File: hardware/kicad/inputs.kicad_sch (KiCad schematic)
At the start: 24 parts, among them U211 EL817, U221 EL817, U231 EL817, U241 EL817, U251 EL817

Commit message: Translate code, hardware and docs to English; bilingual dashboard
- tdm-logic i18n module: every dashboard text in English and Italian,
  chosen by `[display] language` in the profile (English by default, the
  TDM 850 profile keeps Italian); number formatting per language
- Slint fixed labels moved to a `Labels` global filled from the same table;
  `tdm-dash --language en|it`; reference screens regenerated in English with
  Italian check screens
- tdmctl, tdm-dash CLI, simulator scenarios, calibration errors and tools
  print English
- KiCad sheets, WireViz harnesses, perfboard plan and CAD comments in
  English, exports regenerated with the new names
- manual, research, ADRs and READMEs translated; files renamed (docs/manual,
  docs/research, English chapter and ADR names); status markers are now
  [VERIFIED] / [TO VERIFY] / [HYPOTHESIS]

Co-Authored-By: Claude Opus 5.5 <noreply@anthropic.com>
Claude-Session: https://claude.ai/code/session_01G9D4Wshjz9MkaThp4wsrGP
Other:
- note added: "High beam"
- note added: "High beam, turn signals and illumination are active at +12 V: 4.7 kΩ → EL817 LED → ground. Neutral is active to ground (the gearbox switch grounds the wire): +12V_P → 3.3 kΩ → LED → neutral wire. Outputs active low with the Pico's internal pull-up. Wire colours and neutral logic [TO VERIFY] with the bike measurements."
- note added: "Illumination"
- note added: "Left turn signal"
- note added: "Neutral (active to ground)"
- note added: "Outputs to the Pico NEUTRAL → GP6 HIGH_BEAM → GP7 TURN_L → GP8 TURN_R → GP9 ILLUM → GP10"
- note added: "Right turn signal"
- note added: "Warning light inputs"
- note removed: "Abbaglianti"
- note removed: "Abbaglianti, frecce e illuminazione sono attivi a +12 V: 4,7 kΩ → LED dell'EL817 → massa. La folle è attiva verso massa (il contatto del cambio chiude il filo a massa): +12V_P → 3,3 kΩ → LED → filo della folle. Uscite attive basse con pull-up interno del Pico. Colori dei fili e logica della folle [DA VERIFICARE] con i rilievi sulla moto."
- note removed: "Folle (attiva verso massa)"
- note removed: "Freccia destra"
- note removed: "Freccia sinistra"
- note removed: "Illuminazione"
- note removed: "Ingressi delle spie"
- note removed: "Uscite verso il Pico NEUTRAL → GP6 HIGH_BEAM → GP7 TURN_L → GP8 TURN_R → GP9 ILLUM → GP10"
- title: Ingressi delle spie (optoaccoppiatori) -> Warning light inputs (optocouplers)
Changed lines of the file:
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@@
 	(paper "A3")
 	(title_block
-		(title "Ingressi delle spie (optoaccoppiatori)")
+		(title "Warning light inputs (optocouplers)")
 		(date "2026-10-21")
 		(rev "0.1")
 		(company "tdm-dash · CERN-OHL-P-2.0")
-		(comment 1 "Foglio 2 di 8")
-		(comment 2 "Generato da hardware/kicad/generate.py: non modificare a mano")
+		(comment 1 "Sheet 2 of 8")
+		(comment 2 "Generated by hardware/kicad/generate.py: do not edit by hand")
 	)
 	(symbol
@@
 		)
 	)
-	(text "Ingressi delle spie"
+	(text "Warning light inputs"
 		(exclude_from_sim no)
 		(at 10.16 12.7 0)
@@
 		)
 	)
-	(text "Abbaglianti, frecce e illuminazione sono attivi a +12 V: 4,7 kΩ → LED dell'EL817 → massa.\nLa folle è attiva verso massa (il contatto del cambio chiude il filo a massa):\n+12V_P → 3,3 kΩ → LED → filo della folle. Uscite attive basse con pull-up interno del Pico.\nColori dei fili e logica della folle [DA VERIFICARE] con i rilievi sulla moto."
+	(text "High beam, turn signals and illumination are active at +12 V: 4.7 kΩ → EL817 LED → ground.\nNeutral is active to ground (the gearbox switch grounds the wire):\n+12V_P → 3.3 kΩ → LED → neutral wire. Outputs active low with the Pico's internal pull-up.\nWire colours and neutral logic [TO VERIFY] with the bike measurements."
 		(exclude_from_sim no)
 		(at 10.16 17.78 0)
@@
 		)
 	)
-	(text "Abbaglianti"
+	(text "High beam"
 		(exclude_from_sim no)
 		(at 12.7 40.64 0)
@@
 		)
 	)
-	(text "Freccia sinistra"
+	(text "Left turn signal"
 		(exclude_from_sim no)
 		(at 12.7 83.82 0)
@@
 		)
 	)
-	(text "Freccia destra"
+	(text "Right turn signal"
 		(exclude_from_sim no)
 		(at 12.7 127 0)
@@
 		)
 	)
-	(text "Illuminazione"
+	(text "Illumination"
 		(exclude_from_sim no)
 		(at 12.7 170.18 0)
@@
 		)
 	)
-	(text "Folle (attiva verso massa)"
+	(text "Neutral (active to ground)"
 		(exclude_from_sim no)
 		(at 12.7 213.36 0)
@@
 		)
 	)
-	(text "Uscite verso il Pico\nNEUTRAL → GP6\nHIGH_BEAM → GP7\nTURN_L → GP8\nTURN_R → GP9\nILLUM → GP10"
+	(text "Outputs to the Pico\nNEUTRAL → GP6\nHIGH_BEAM → GP7\nTURN_L → GP8\nTURN_R → GP9\nILLUM → GP10"
 		(exclude_from_sim no)
 		(at 190.5 50.8 0)

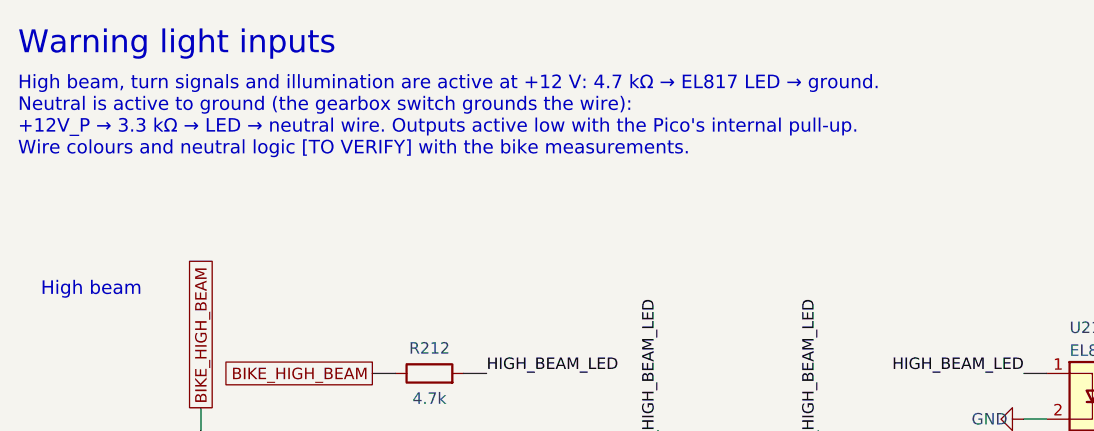
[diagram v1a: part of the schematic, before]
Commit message: English README, ADR 0012, CLAUDE.md rules, banner; consistent spelling
- README and docs/assets in English, banner tagline "Open-source digital
  instrument cluster" and regenerated banner
- ADR 0012: English repository, bilingual dashboard
- CLAUDE.md: English everywhere, dashboard texts in both languages through
  tdm-logic i18n, new status markers
- American spelling across docs, harness labels and schematic notes;
  ADR 0007 renamed to 0007-licenses; exports and screens regenerated

Co-Authored-By: Claude Opus 5.5 <noreply@anthropic.com>
Claude-Session: https://claude.ai/code/session_01G9D4Wshjz9MkaThp4wsrGP
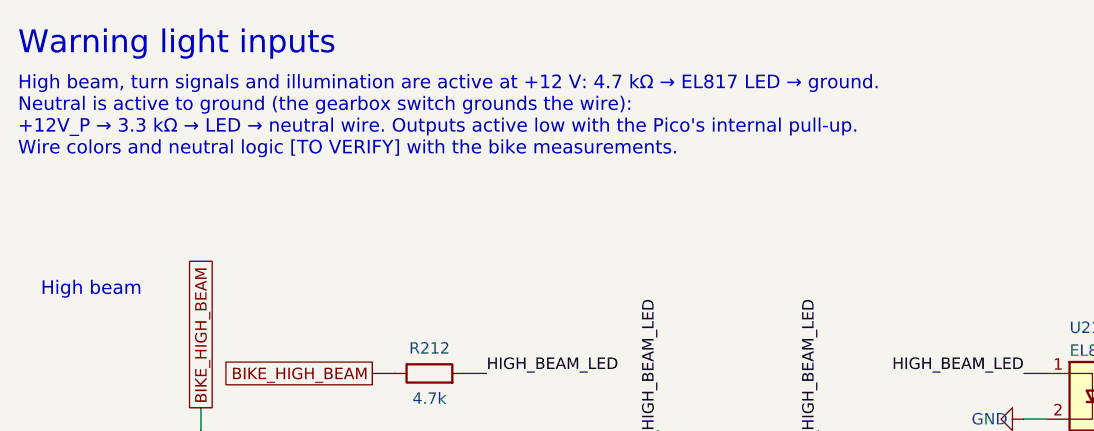
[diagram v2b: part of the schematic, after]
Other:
- note added: "High beam, turn signals and illumination are active at +12 V: 4.7 kΩ → EL817 LED → ground. Neutral is active to ground (the gearbox switch grounds the wire): +12V_P → 3.3 kΩ → LED → neutral wire. Outputs active low with the Pico's internal pull-up. Wire colors and neutral logic [TO VERIFY] with the bike measurements."
- note removed: "High beam, turn signals and illumination are active at +12 V: 4.7 kΩ → EL817 LED → ground. Neutral is active to ground (the gearbox switch grounds the wire): +12V_P → 3.3 kΩ → LED → neutral wire. Outputs active low with the Pico's internal pull-up. Wire colours and neutral logic [TO VERIFY] with the bike measurements."
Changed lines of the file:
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@@
 		)
 	)
-	(text "High beam, turn signals and illumination are active at +12 V: 4.7 kΩ → EL817 LED → ground.\nNeutral is active to ground (the gearbox switch grounds the wire):\n+12V_P → 3.3 kΩ → LED → neutral wire. Outputs active low with the Pico's internal pull-up.\nWire colours and neutral logic [TO VERIFY] with the bike measurements."
+	(text "High beam, turn signals and illumination are active at +12 V: 4.7 kΩ → EL817 LED → ground.\nNeutral is active to ground (the gearbox switch grounds the wire):\n+12V_P → 3.3 kΩ → LED → neutral wire. Outputs active low with the Pico's internal pull-up.\nWire colors and neutral logic [TO VERIFY] with the bike measurements."
 		(exclude_from_sim no)
 		(at 10.16 17.78 0)

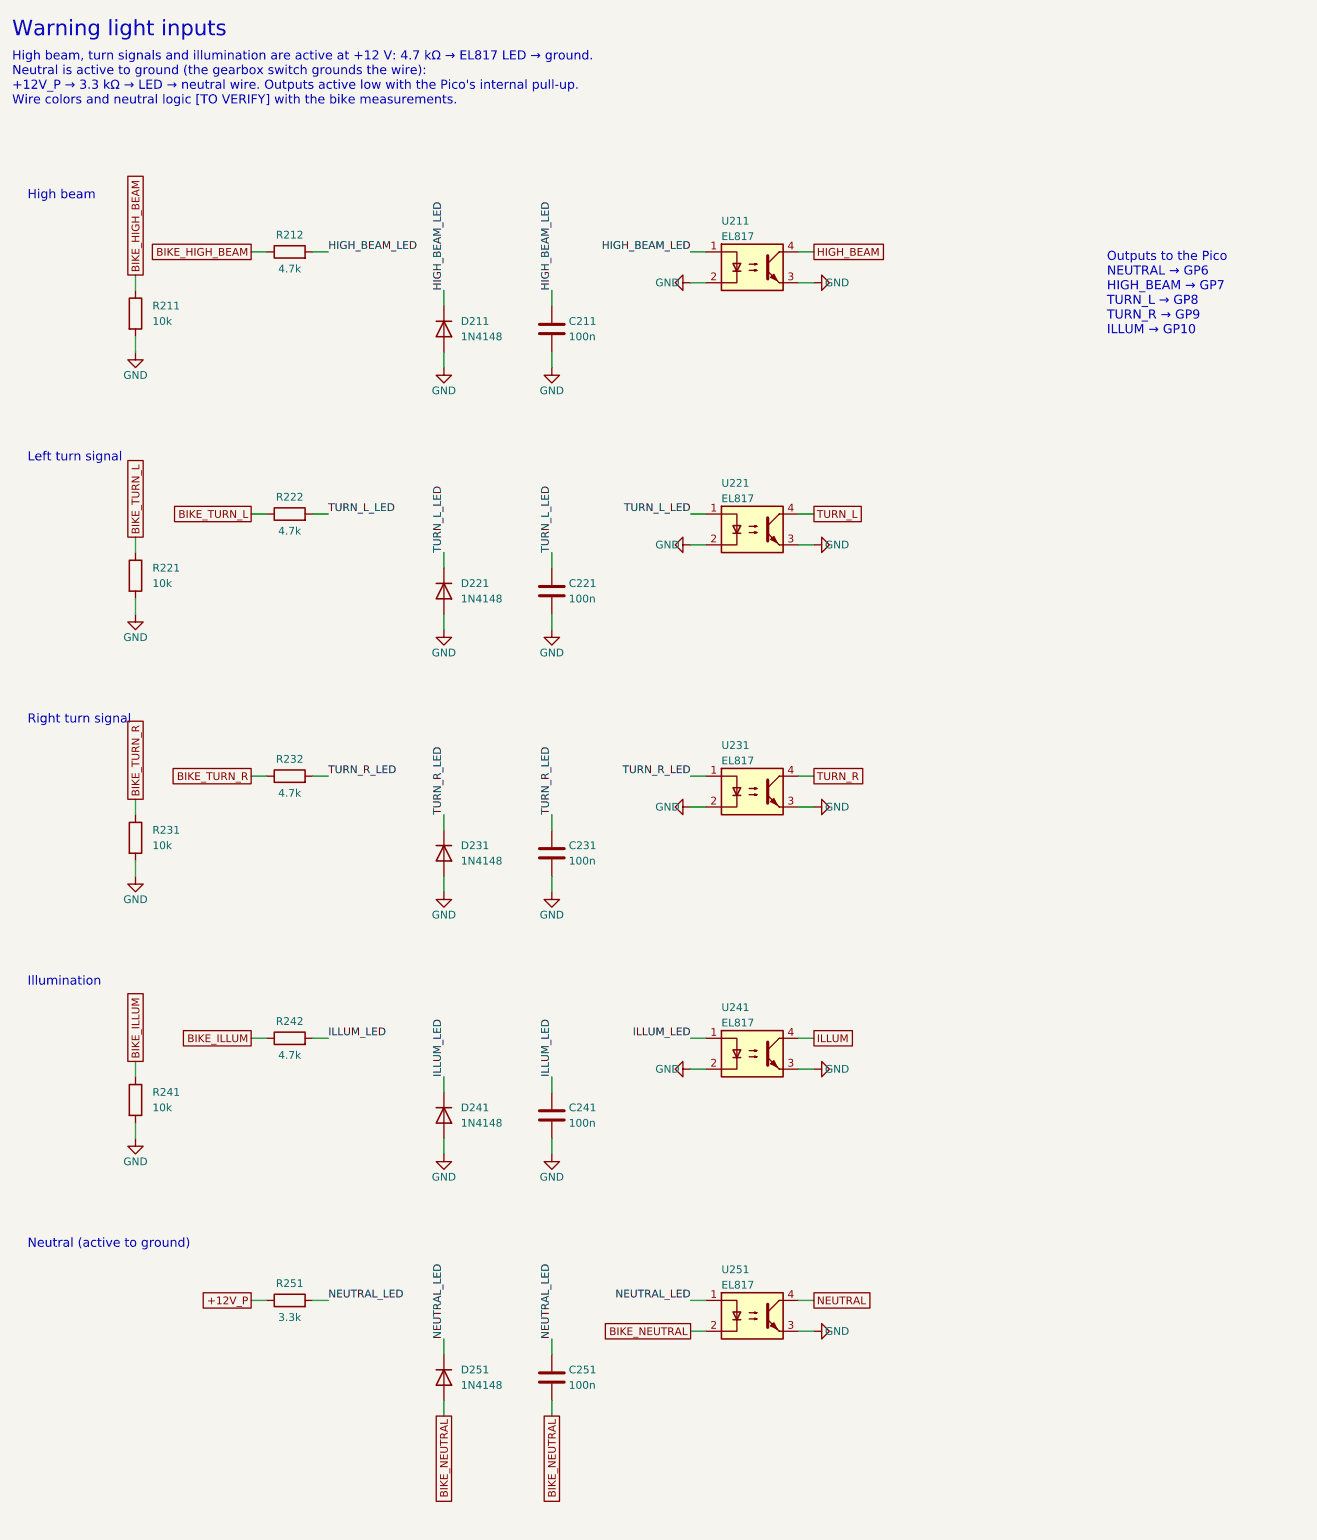
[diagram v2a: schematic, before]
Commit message: Schematic: drawn wires, block diagram, new title block
The sheets were a netlist in disguise: every pin ended in a short stub and
a label, so the circuits had to be pieced together by name, labels
overlapped, two sheets fell off the index page and the title block was
KiCad's default. The generator now draws the schematic:

- hardware/kicad/schgen: placement on the 50 mil grid, orthogonal wires,
  junctions, hierarchical ports, module and connector symbols with named
  pins; the drawing is normalised the way KiCad 9 reads it and checked
  against the declared netlist (no wire may connect anything else)
- hardware/kicad/sheets: one module per sheet, laid out left to right
  from the bike to the Pico; the root sheet is a block diagram whose
  wires are the signals between sheets
- tdm-dash.kicad_wks: frame and title block of the project
- symbols copied from KiCad 9.0.9 (vendor_symbols.py): the generator no
  longer needs KiCad installed
- export.sh: ERC, tools/check_netlist.py (KiCad's netlist is the declared
  one), check_pinmap.py, PDF and SVG on white, tools/check_svg_layout.py
  (no text over another text, a wire, the frame or the title block)

The circuit is unchanged: KiCad's netlist of the old and new schematic
has the same 56 nets (FRAM pins now follow the breakout header, R603/R604
pins swapped).

Co-Authored-By: Claude Opus 5.5 <noreply@anthropic.com>
Claude-Session: https://claude.ai/code/session_01G9D4Wshjz9MkaThp4wsrGP
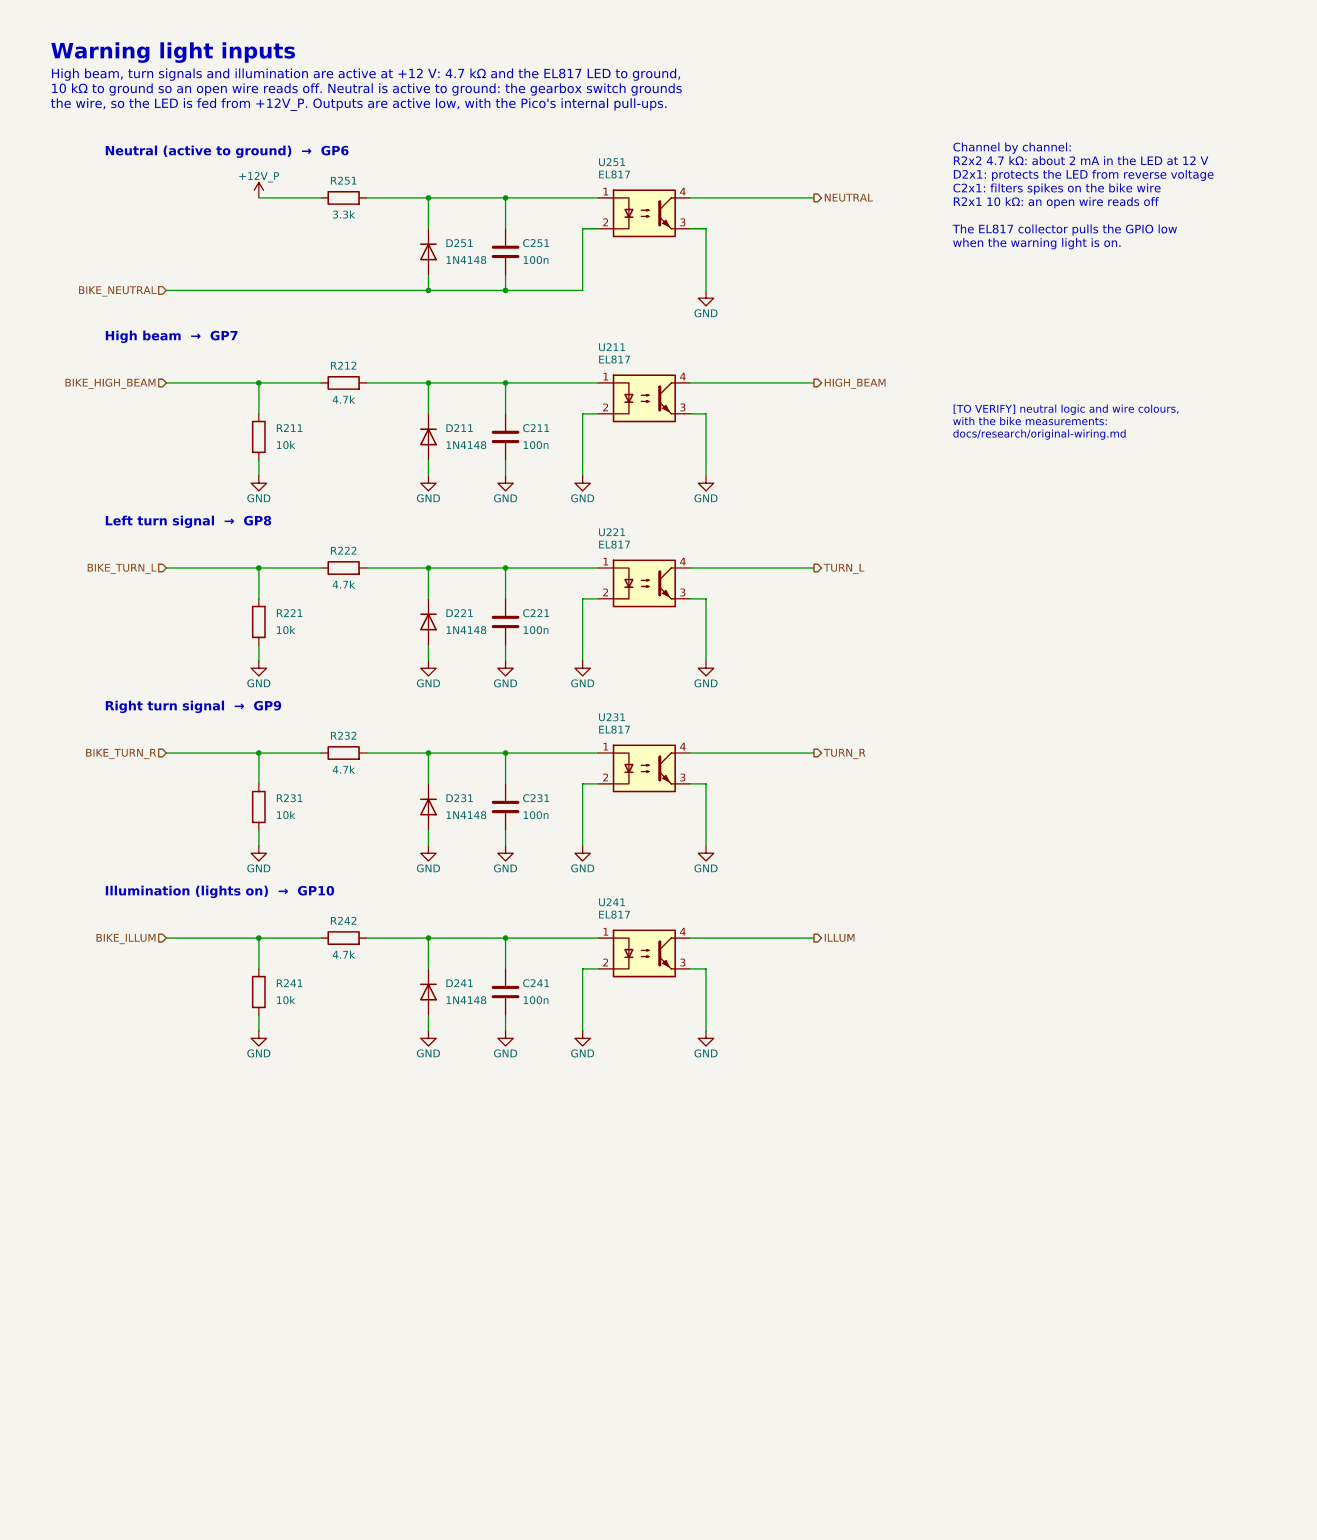
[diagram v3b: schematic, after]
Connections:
- net HIGH_BEAM_LED: no longer names the net of C211.1, D211.1 (K), R212.2, U211.1
- net ILLUM_LED: no longer names the net of C241.1, D241.1 (K), R242.2, U241.1
- net NEUTRAL_LED: no longer names the net of C251.1, D251.1 (K), R251.2, U251.1
- net TURN_L_LED: no longer names the net of C221.1, D221.1 (K), R222.2, U221.1
- net TURN_R_LED: no longer names the net of C231.1, D231.1 (K), R232.2, U231.1
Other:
- note added: "Channel by channel: R2x2 4.7 kΩ: about 2 mA in the LED at 12 V D2x1: protects the LED from reverse voltage C2x1: filters spikes on the bike wire R2x1 10 kΩ: an open wire reads off The EL817 collector pulls the GPIO low when the warning light is on."
- note added: "High beam → GP7"
- note added: "High beam, turn signals and illumination are active at +12 V: 4.7 kΩ and the EL817 LED to ground, 10 kΩ to ground so an open wire reads off. Neutral is active to ground: the gearbox switch grounds the wire, so the LED is fed from +12V_P. Outputs are active low, with the Pico's internal pull-ups."
- note added: "Illumination (lights on) → GP10"
- note added: "Left turn signal → GP8"
- note added: "Neutral (active to ground) → GP6"
- note added: "Right turn signal → GP9"
- note added: "[TO VERIFY] neutral logic and wire colours, with the bike measurements: docs/research/original-wiring.md"
- note removed: "High beam"
- note removed: "High beam, turn signals and illumination are active at +12 V: 4.7 kΩ → EL817 LED → ground. Neutral is active to ground (the gearbox switch grounds the wire): +12V_P → 3.3 kΩ → LED → neutral wire. Outputs active low with the Pico's internal pull-up. Wire colors and neutral logic [TO VERIFY] with the bike measurements."
- note removed: "Illumination"
- note removed: "Left turn signal"
- note removed: "Neutral (active to ground)"
- note removed: "Outputs to the Pico NEUTRAL → GP6 HIGH_BEAM → GP7 TURN_L → GP8 TURN_R → GP9 ILLUM → GP10"
- note removed: "Right turn signal"
- company: tdm-dash · CERN-OHL-P-2.0 -> tdm-dash

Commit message: Schematic: backlight breakout off the board, harness fuse, micro-USB plug
The perfboard has no room for the TPS61169 breakout, and the build steps
already wired it off the board: J701 now gives it +5 V, CTRL and ground,
and its output goes to the panel LED pins (J704), in a dashed box like the
buttons. F101 is marked as the inline fuse of the adapter harness, J401 as
the terminal for the sensor cable, and J703 has the five pins of the
micro-USB plug, with ID tied to ground.

Co-Authored-By: Claude Opus 5.5 <noreply@anthropic.com>
Claude-Session: https://claude.ai/code/session_01G9D4Wshjz9MkaThp4wsrGP
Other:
- note added: "[TO VERIFY] neutral logic and wire colors, with the bike measurements: docs/research/original-wiring.md"
- note removed: "[TO VERIFY] neutral logic and wire colours, with the bike measurements: docs/research/original-wiring.md"
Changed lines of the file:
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@@
 		)
 	)
-	(text "[TO VERIFY] neutral logic and wire colours,\nwith the bike measurements:\ndocs/research/original-wiring.md"
+	(text "[TO VERIFY] neutral logic and wire colors,\nwith the bike measurements:\ndocs/research/original-wiring.md"
 		(exclude_from_sim no)
 		(at 165.1 76.2 0)
